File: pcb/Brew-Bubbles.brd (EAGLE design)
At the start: 25.5 x 28.7 mm, 7 parts, among them U1 GP1A57HR, U2 WEMOS-D1-MINI

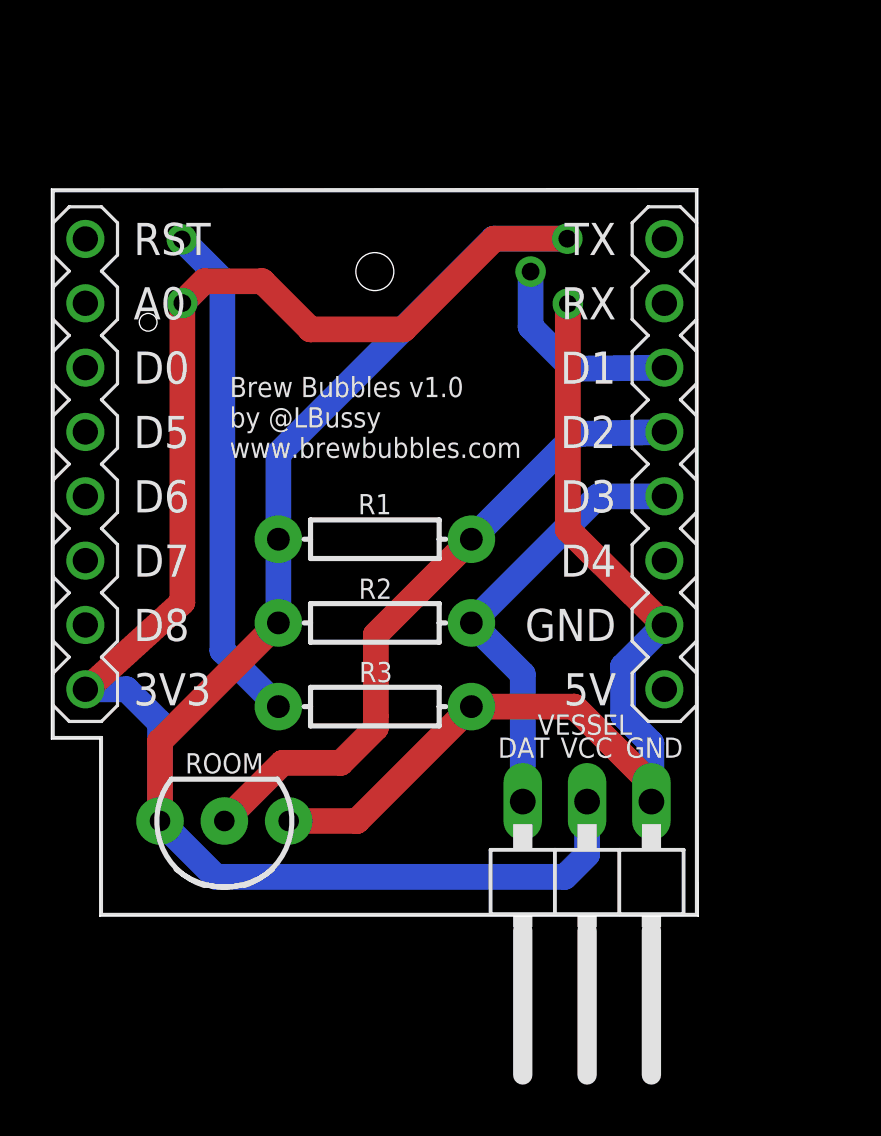
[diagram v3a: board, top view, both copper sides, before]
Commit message: Updates to trace routes
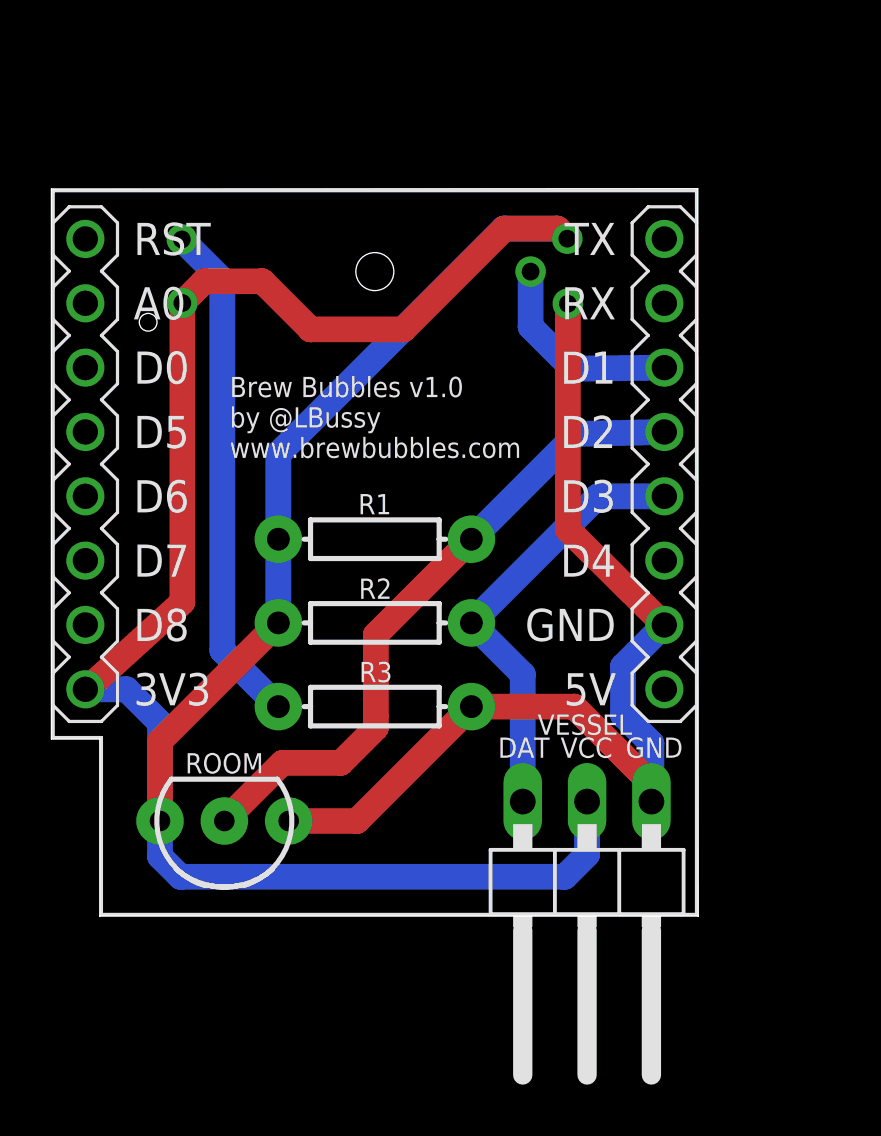
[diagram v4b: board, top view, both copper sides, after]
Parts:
- R1, R2: value 330 -> 2.2kΩ
- R3: value 330 -> 150Ω
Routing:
- net 3V3: track 93.8 -> 95.3 mm
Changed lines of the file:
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@@
 <drawing>
 <settings>
-<setting alwaysvectorfont="no"/>
+<setting alwaysvectorfont="yes"/>
 <setting verticaltext="up"/>
 </settings>
@@
 </element>
 <element name="U2" library="diy-modules" package="WEMOS-D1-MINI-SHIELD" value="WEMOS-D1-MINI" x="12.8" y="14.7" smashed="yes"/>
-<element name="R1" library="SparkFun-Resistors" package="AXIAL-0.3" value="330" x="12.8013" y="14.91" smashed="yes" rot="R180">
+<element name="R1" library="SparkFun-Resistors" package="AXIAL-0.3" value="2.2kΩ" x="12.8013" y="14.91" smashed="yes" rot="R180">
 <attribute name="NAME" x="12.1413" y="16.694" size="0.8" layer="25" font="vector" ratio="14" rot="R180" align="bottom-right"/>
 <attribute name="PROD_ID" value="RES-8371" x="12.8013" y="14.91" size="1.778" layer="27" rot="R180" display="off"/>
@@
 <attribute name="POPULARITY" value="17" x="21.18" y="0.74" size="1.778" layer="27" rot="R180" display="off"/>
 </element>
-<element name="R2" library="SparkFun-Resistors" package="AXIAL-0.3" value="330" x="12.8013" y="11.6054" smashed="yes" rot="R180">
+<element name="R2" library="SparkFun-Resistors" package="AXIAL-0.3" value="2.2kΩ" x="12.8013" y="11.6054" smashed="yes" rot="R180">
 <attribute name="NAME" x="12.1625" y="13.356" size="0.8" layer="25" font="vector" ratio="14" rot="R180" align="bottom-right"/>
 <attribute name="PROD_ID" value="RES-8371" x="12.8013" y="11.6054" size="1.778" layer="27" rot="R180" display="off"/>
@@
 <attribute name="SF_ID" value="SEN-09299" x="12.8" y="25.4762" size="1.778" layer="28" rot="MR180" display="off"/>
 </element>
-<element name="R3" library="SparkFun-Resistors" package="AXIAL-0.3" value="330" x="12.8013" y="8.3008" smashed="yes" rot="R180">
+<element name="R3" library="SparkFun-Resistors" package="AXIAL-0.3" value="150Ω" x="12.8013" y="8.3008" smashed="yes" rot="R180">
 <attribute name="NAME" x="12.1813" y="10.0648" size="0.8" layer="25" font="vector" ratio="14" rot="R180" align="bottom-right"/>
 <attribute name="PROD_ID" value="RES-8371" x="12.8013" y="8.3008" size="1.778" layer="27" rot="R180" display="off"/>
@@
 <contactref element="R1" pad="P$2"/>
 <contactref element="ROOM" pad="3"/>
-<wire x1="17.4894" y1="26.7762" x2="8.9913" y2="18.2781" width="1.016" layer="16"/>
+<wire x1="17.8894" y1="27.1762" x2="8.9913" y2="18.2781" width="1.016" layer="16"/>
 <wire x1="8.9913" y1="14.91" x2="8.9913" y2="18.2781" width="1.016" layer="16"/>
-<wire x1="17.4894" y1="26.7762" x2="20.4" y2="26.7762" width="1.016" layer="16"/>
+<wire x1="20" y1="27.1762" x2="20.4" y2="26.7762" width="1.016" layer="16"/>
+<wire x1="20" y1="27.1762" x2="17.8894" y2="27.1762" width="1.016" layer="16"/>
 <wire x1="5.2" y1="24.2362" x2="5.2" y2="12.42035" width="1.016" layer="1"/>
 <wire x1="5.2" y1="12.42035" x2="1.37383125" y2="8.9408" width="1.016" layer="1"/>
@@
 <wire x1="8.3556" y1="25.0962" x2="10.2588" y2="23.193" width="1.016" layer="1"/>
 <wire x1="10.2588" y1="23.193" x2="13.933" y2="23.193" width="1.016" layer="1"/>
-<wire x1="17.5162" y1="26.7762" x2="20.4" y2="26.7762" width="1.016" layer="1"/>
-<wire x1="13.933" y1="23.193" x2="17.5162" y2="26.7762" width="1.016" layer="1"/>
+<wire x1="20" y1="27.1762" x2="20.4" y2="26.7762" width="1.016" layer="1"/>
+<wire x1="20" y1="27.1762" x2="17.9162" y2="27.1762" width="1.016" layer="1"/>
+<wire x1="13.933" y1="23.193" x2="17.9162" y2="27.1762" width="1.016" layer="1"/>
 <contactref element="VESSEL" pad="2"/>
 <wire x1="8.9913" y1="14.91" x2="8.9913" y2="11.6054" width="1.016" layer="16"/>
@@
 <wire x1="4.318" y1="7.662" x2="4.318" y2="3.7846" width="1.016" layer="16"/>
 <wire x1="2.995" y1="8.985" x2="4.318" y2="7.662" width="1.016" layer="16"/>
-<wire x1="4.318" y1="3.7846" x2="6.5226" y2="1.58" width="1.016" layer="16"/>
+<wire x1="5.1226" y1="1.58" x2="4.318" y2="2.3846" width="1.016" layer="16"/>
+<wire x1="4.318" y1="3.7846" x2="4.318" y2="2.3846" width="1.016" layer="16"/>
 <wire x1="20.3" y1="1.58" x2="21.18" y2="2.46" width="1.016" layer="16"/>
 <wire x1="21.18" y1="2.46" x2="21.18" y2="4.55" width="1.016" layer="16"/>
-<wire x1="6.5226" y1="1.58" x2="20.3" y2="1.58" width="1.016" layer="16"/>
+<wire x1="5.1226" y1="1.58" x2="20.3" y2="1.58" width="1.016" layer="16"/>
 </signal>
 <signal name="D2">

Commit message: Remove onboard sensor move to lead
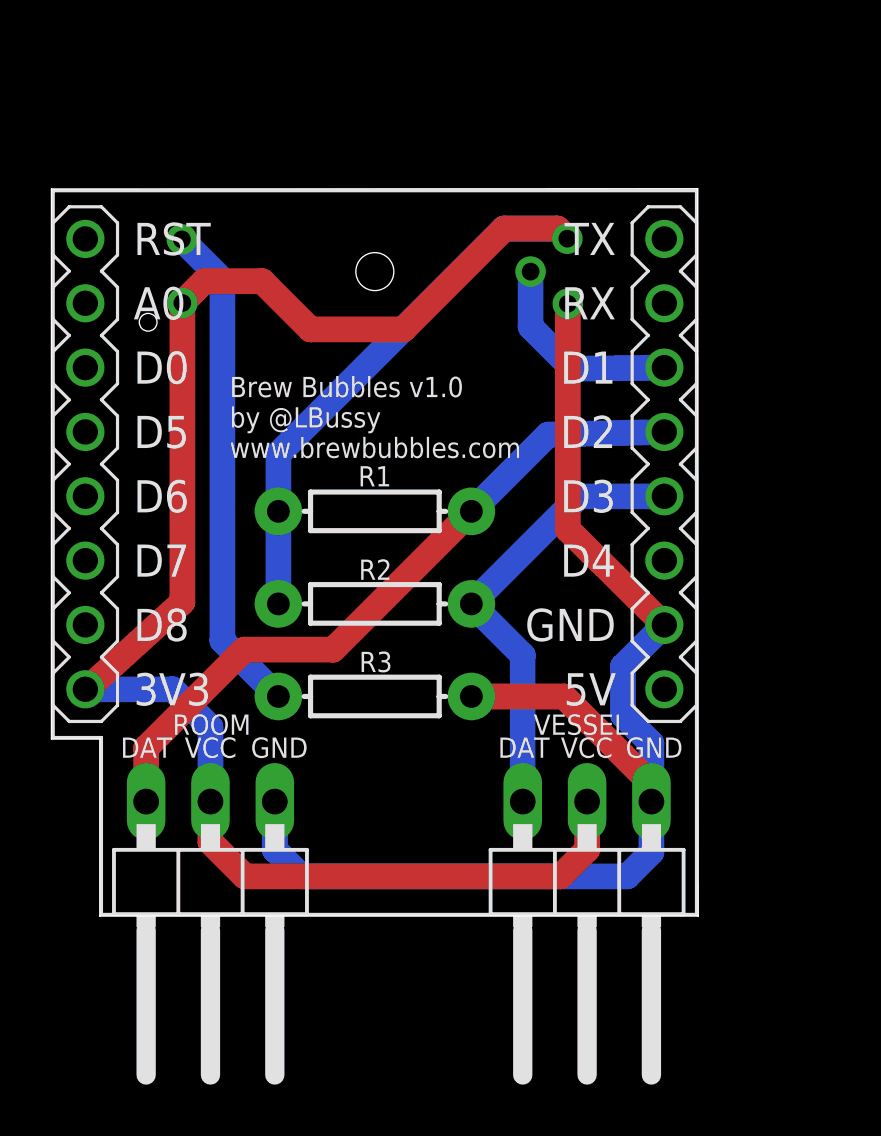
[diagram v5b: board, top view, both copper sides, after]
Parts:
- ROOM: value DS18B20 -> 3PIN90; device SparkFun-Sensors:TO-92-AMMO -> pinhead:1X03/90
- moved ROOM 3.09 mm to (6.31, 0.74)
- moved R1 1.10 mm to (12.8, 16.0)
- moved R2 0.75 mm to (12.8, 12.4)
- moved R3 0.40 mm to (12.8, 8.70)
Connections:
- net 3V3: now also ROOM.2; no longer ROOM.3
- net D2: now also ROOM.3; no longer ROOM.2
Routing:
- net 3V3: track 95.3 -> 84.2 mm
- net GND: track 40.5 -> 51.2 mm
- net D2: track 25.9 -> 27.7 mm

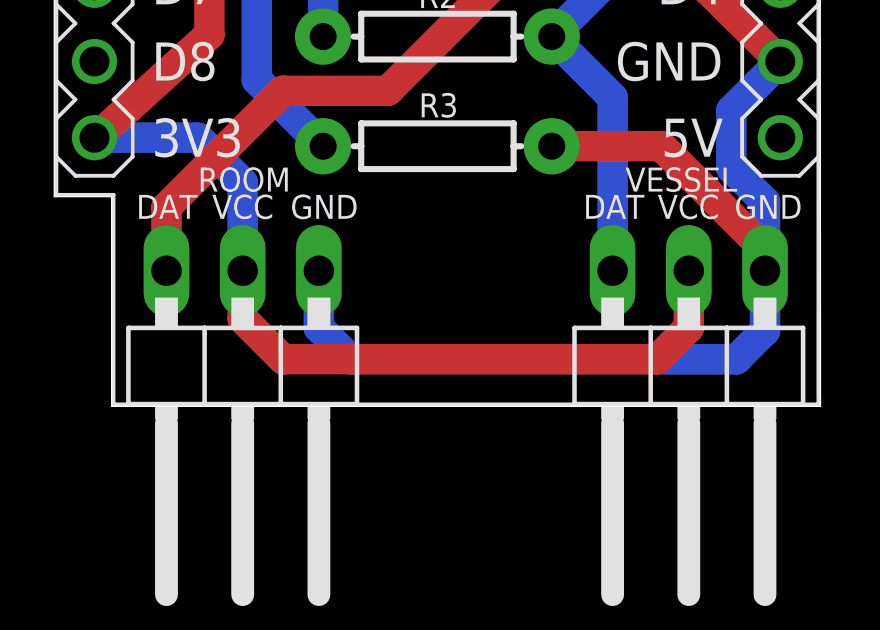
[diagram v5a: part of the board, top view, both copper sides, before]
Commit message: Change DS18B20 for ROOM to waterproof lead
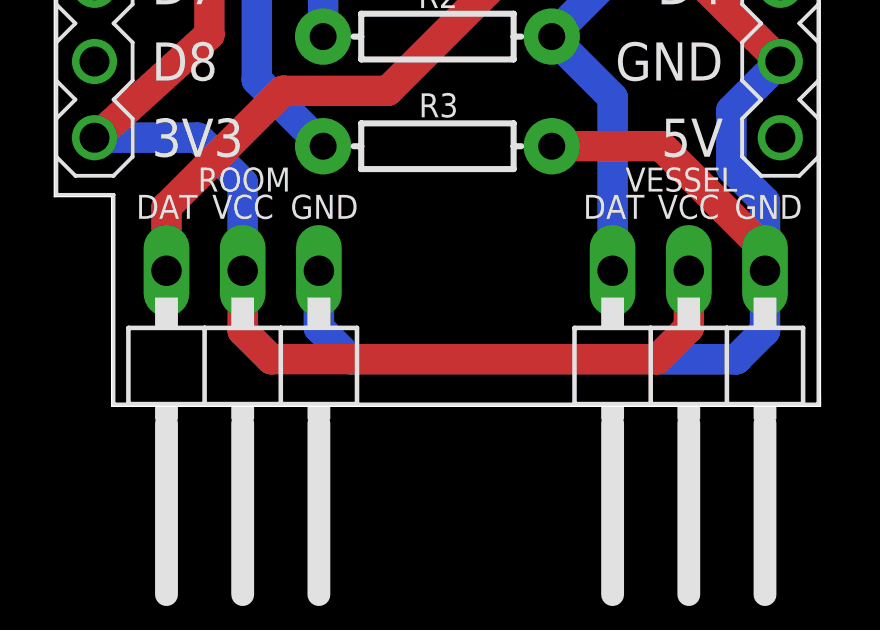
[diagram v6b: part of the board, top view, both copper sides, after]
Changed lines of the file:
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@@
 <drawing>
 <settings>
-<setting alwaysvectorfont="yes"/>
+<setting alwaysvectorfont="no"/>
 <setting verticaltext="up"/>
 </settings>
@@
 <wire x1="16.6113" y1="8.7008" x2="20.2692" y2="8.7008" width="1.016" layer="1"/>
 <wire x1="23.72" y1="5.25" x2="20.2692" y2="8.7008" width="1.016" layer="1"/>
-<contactref element="ROOM" pad="1"/>
 <contactref element="VESSEL" pad="1"/>
 <wire x1="23.72" y1="4.55" x2="23.72" y2="5.25" width="1.016" layer="1"/>
 <wire x1="9.9" y1="1.6" x2="8.85" y2="2.65" width="1.016" layer="16"/>
-<wire x1="8.85" y1="4.55" x2="8.85" y2="2.65" width="1.016" layer="16"/>
 <wire x1="23.72" y1="2.55" x2="23.72" y2="4.55" width="1.016" layer="16"/>
 <wire x1="23.72" y1="2.55" x2="22.77" y2="1.6" width="1.016" layer="16"/>
 <wire x1="9.9" y1="1.6" x2="22.77" y2="1.6" width="1.016" layer="16"/>
 <wire x1="23.72" y1="6.85" x2="23.72" y2="4.55" width="1.016" layer="16"/>
+<contactref element="ROOM" pad="1"/>
+<wire x1="8.85" y1="2.65" x2="8.85" y2="4.55" width="1.016" layer="16"/>
 </signal>
 <signal name="3V3">
@@
 <wire x1="8.9913" y1="16.01" x2="8.9913" y2="12.3554" width="1.016" layer="16"/>
 <contactref element="ROOM" pad="2"/>
-<wire x1="6.31" y1="4.55" x2="6.31" y2="2.95" width="1.016" layer="1"/>
-<wire x1="7.66" y1="1.6" x2="6.31" y2="2.95" width="1.016" layer="1"/>
+<wire x1="6.31" y1="4.55" x2="6.31" y2="2.55" width="1.016" layer="1"/>
+<wire x1="7.26" y1="1.6" x2="6.31" y2="2.55" width="1.016" layer="1"/>
 <wire x1="21.18" y1="2.65" x2="21.18" y2="4.55" width="1.016" layer="1"/>
 <wire x1="21.18" y1="2.65" x2="20.13" y2="1.6" width="1.016" layer="1"/>
-<wire x1="7.66" y1="1.6" x2="20.13" y2="1.6" width="1.016" layer="1"/>
+<wire x1="7.26" y1="1.6" x2="20.13" y2="1.6" width="1.016" layer="1"/>
 <wire x1="1.37" y1="8.985" x2="4.815" y2="8.985" width="1.016" layer="16"/>
 <wire x1="6.31" y1="7.49" x2="6.31" y2="4.55" width="1.016" layer="16"/>

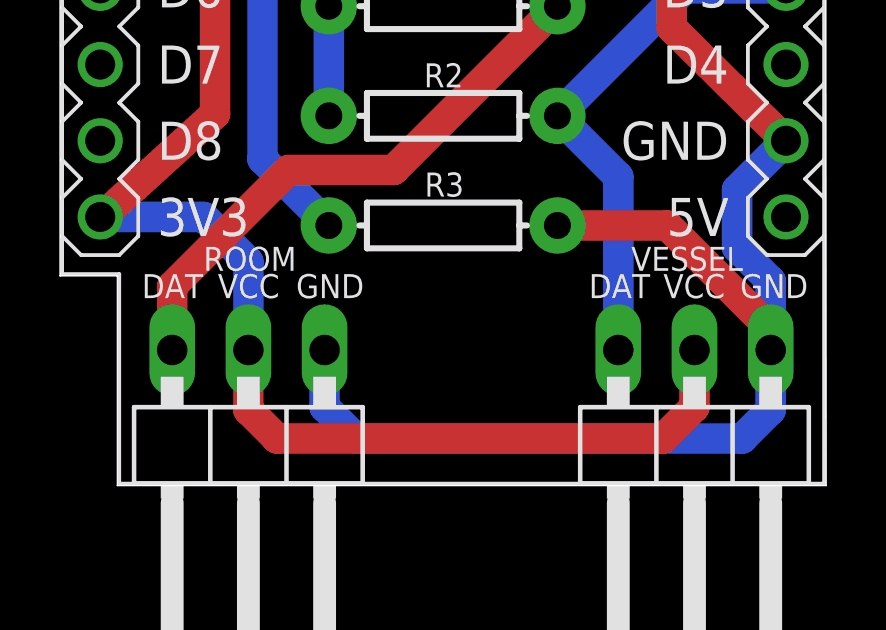
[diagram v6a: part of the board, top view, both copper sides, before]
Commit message: Update PCB to show sensor pins on back
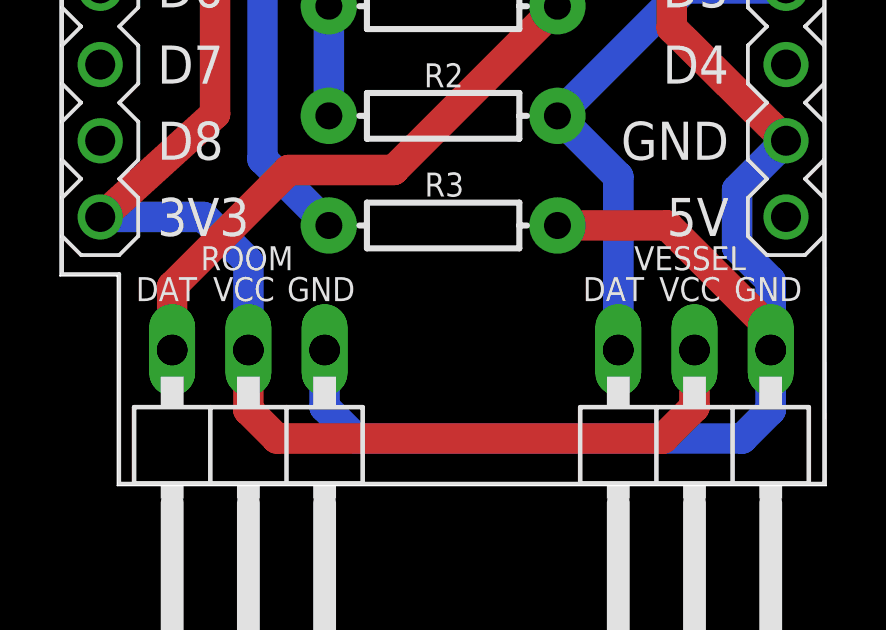
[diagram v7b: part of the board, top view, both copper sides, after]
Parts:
- added ROOM1, VESSEL1: 3PIN90, pinhead:1X03/90
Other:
- board text added: "ROOM"
- board text added: "VESSEL"
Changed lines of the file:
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@@
 <?xml version="1.0" encoding="utf-8"?>
 <!DOCTYPE eagle SYSTEM "eagle.dtd">
-<eagle version="9.4.2">
+<eagle version="9.5.0">
 <drawing>
 <settings>
@@
 by @LBussy
 www.brewbubbles.com</text>
-<text x="17.66" y="6.28" size="0.8" layer="25">DAT</text>
-<text x="20.1421" y="6.28" size="0.8" layer="25">VCC</text>
-<text x="22.7" y="6.28" size="0.8" layer="25">GND</text>
+<text x="17.46" y="6.18" size="0.8" layer="25">DAT</text>
+<text x="20.0021" y="6.18" size="0.8" layer="25">VCC</text>
+<text x="22.5" y="6.18" size="0.8" layer="25">GND</text>
 <wire x1="25.55" y1="28.75" x2="25.57" y2="0.03" width="0" layer="20"/>
-<text x="2.76" y="6.28" size="0.8" layer="25">DAT</text>
-<text x="5.2921" y="6.28" size="0.8" layer="25">VCC</text>
-<text x="7.9" y="6.28" size="0.8" layer="25">GND</text>
+<text x="2.56" y="6.18" size="0.8" layer="25">DAT</text>
+<text x="5.1321" y="6.18" size="0.8" layer="25">VCC</text>
+<text x="7.6" y="6.18" size="0.8" layer="25">GND</text>
+<text x="4.97" y="6.18" size="0.8" layer="26" rot="MR0">DAT</text>
+<text x="7.4621" y="6.18" size="0.8" layer="26" rot="MR0">VCC</text>
+<text x="10.15" y="6.18" size="0.8" layer="26" rot="MR0">GND</text>
+<text x="8.03" y="7.21" size="0.8" layer="26" rot="MR0">ROOM</text>
+<text x="19.77" y="6.18" size="0.8" layer="26" rot="MR0">DAT</text>
+<text x="22.2621" y="6.18" size="0.8" layer="26" rot="MR0">VCC</text>
+<text x="24.95" y="6.18" size="0.8" layer="26" rot="MR0">GND</text>
+<text x="23.33" y="7.21" size="0.8" layer="26" rot="MR0">VESSEL</text>
 </plain>
 <attributes>
@@
 </element>
 <element name="VESSEL" library="pinhead" library_urn="urn:adsk.eagle:library:325" package="1X03/90" package3d_urn="urn:adsk.eagle:package:22459/2" value="3PIN90" x="21.18" y="0.74" smashed="yes" rot="R180">
-<attribute name="NAME" x="19.0674" y="7.1888" size="0.8" layer="25" font="vector" ratio="10"/>
+<attribute name="NAME" x="19.1674" y="7.21" size="0.8" layer="25" font="vector" ratio="10"/>
 <attribute name="POPULARITY" value="17" x="21.18" y="0.74" size="1.778" layer="27" rot="R180" display="off"/>
 </element>
@@
 </element>
 <element name="ROOM" library="pinhead" library_urn="urn:adsk.eagle:library:325" package="1X03/90" package3d_urn="urn:adsk.eagle:package:22459/2" value="3PIN90" x="6.31" y="0.74" smashed="yes" rot="R180">
-<attribute name="NAME" x="4.815" y="7.1888" size="0.8" layer="25" ratio="10"/>
+<attribute name="NAME" x="4.715" y="7.21" size="0.8" layer="25" ratio="10"/>
 <attribute name="POPULARITY" value="17" x="6.31" y="0.74" size="1.778" layer="27" rot="R180" display="off"/>
 </element>
+<element name="ROOM1" library="pinhead" library_urn="urn:adsk.eagle:library:325" package="1X03/90" package3d_urn="urn:adsk.eagle:package:22459/2" value="3PIN90" x="6.31" y="0.74" smashed="yes" rot="MR180">
+<attribute name="POPULARITY" value="17" x="6.31" y="0.74" size="1.778" layer="28" rot="MR180" display="off"/>
+</element>
+<element name="VESSEL1" library="pinhead" library_urn="urn:adsk.eagle:library:325" package="1X03/90" package3d_urn="urn:adsk.eagle:package:22459/2" value="3PIN90" x="21.18" y="0.74" smashed="yes" rot="MR180">
+<attribute name="POPULARITY" value="17" x="21.18" y="0.74" size="1.778" layer="28" rot="MR180" display="off"/>
+</element>
 </elements>
